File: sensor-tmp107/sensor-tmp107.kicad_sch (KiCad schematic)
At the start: 13 parts, among them J1 DE9_Socket_MountingHoles, J2 DE9_Socket_MountingHoles, Q1 MMBT3904, Q2 MMBT3904, U1 TMP107BIDR

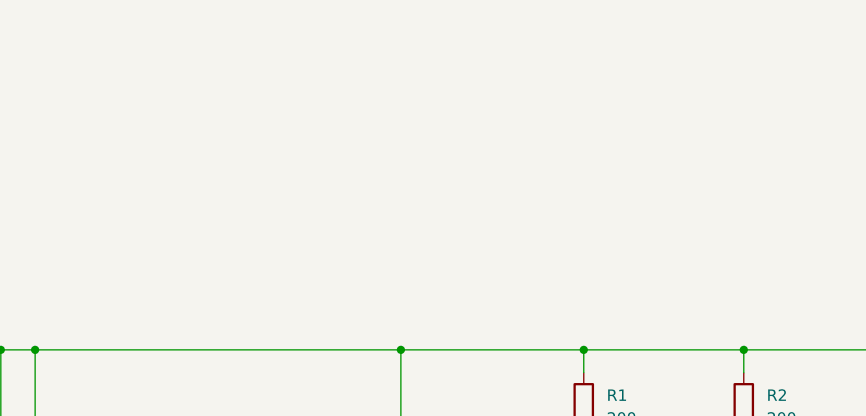
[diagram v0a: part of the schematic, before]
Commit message: Rework pcb to make it easier to attach mechanically
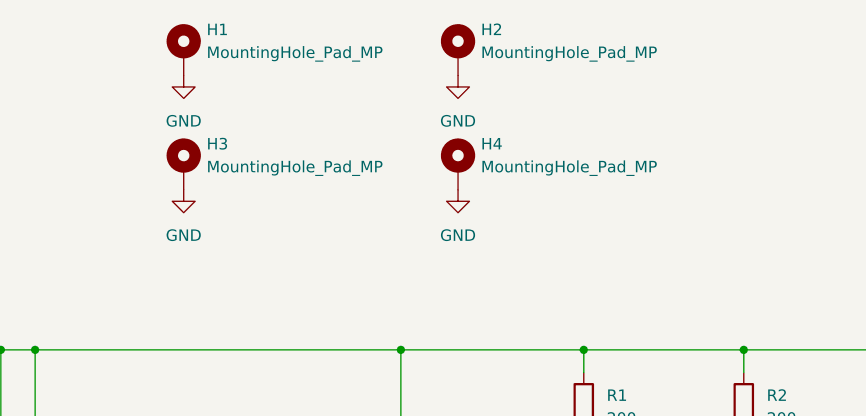
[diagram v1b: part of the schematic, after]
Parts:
- added H1, H2, H3, H4: MountingHole_Pad_MP, MountingHole:MountingHole_6.4mm_M6, symbol Mechanical:MountingHole_Pad_MP
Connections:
- net GND: now also H1.MP, H2.MP, H3.MP, H4.MP
